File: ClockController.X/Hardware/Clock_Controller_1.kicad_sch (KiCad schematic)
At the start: 3 parts, among them U1 PIC16F15224-I/SL

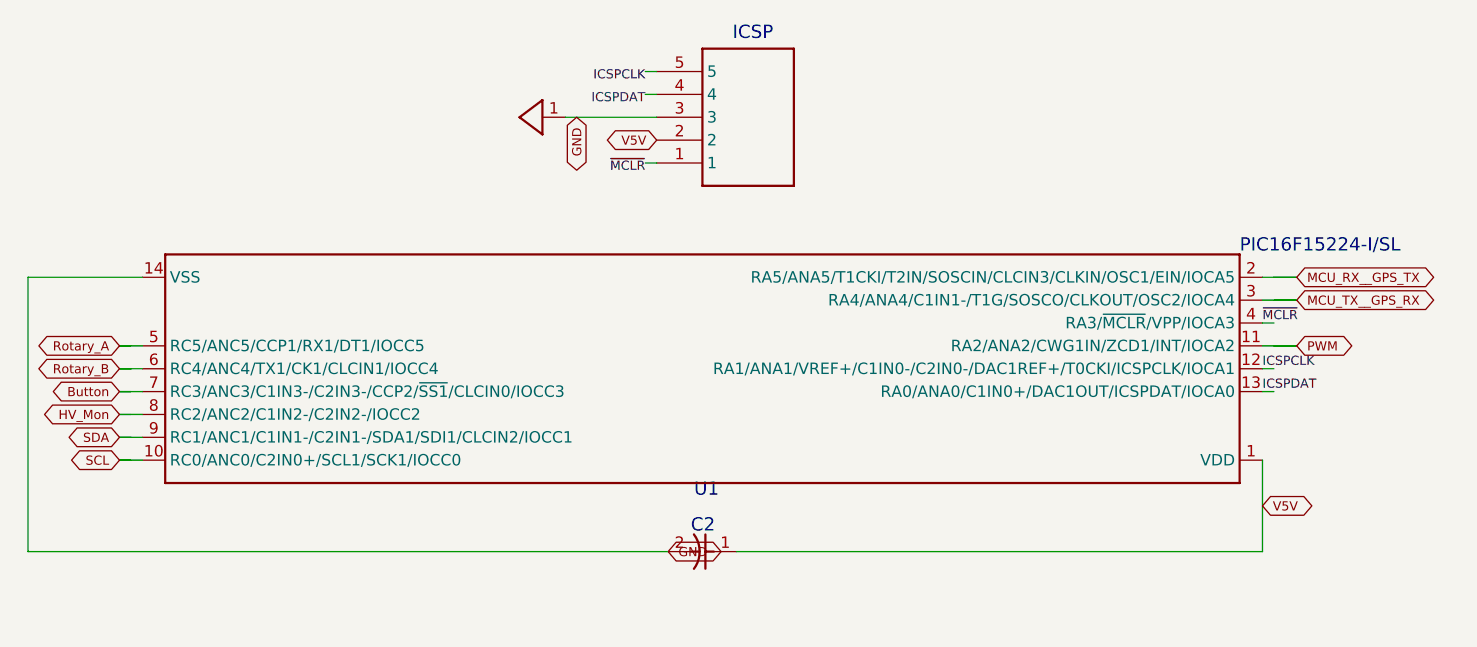
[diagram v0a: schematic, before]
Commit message: Cleaned up a bunch of labels
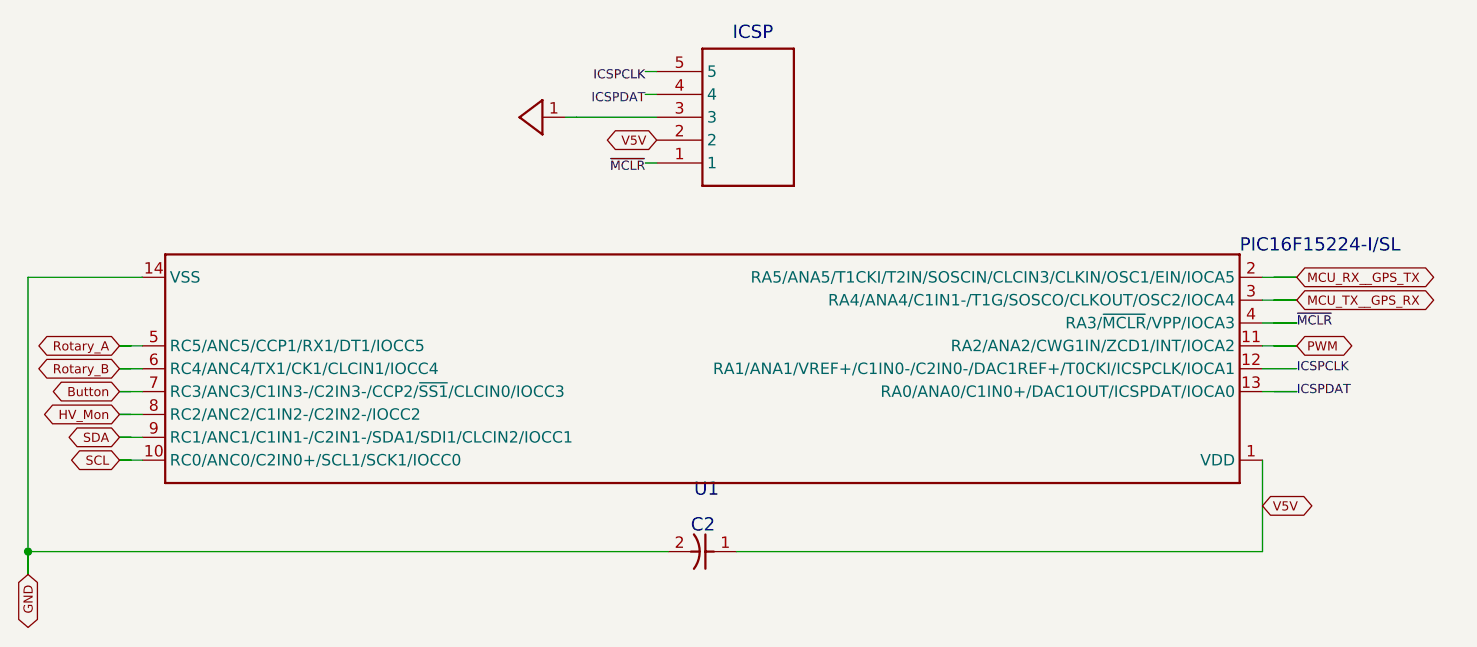
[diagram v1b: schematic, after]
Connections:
- net GND_DIGITAL: no longer C2.2, U1.14 (VSS)
- new net GND: C2.2, U1.14 (VSS)
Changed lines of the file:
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@@
 	(generator_version "8.0")
 	(paper "A4")
+	(junction
+		(at 68.58 130.81)
+		(diameter 0)
+		(color 0 0 0 0)
+	)
+	(wire
+		(pts
+			(xy 68.58 130.81) (xy 139.7 130.81)
+		)
+		(stroke
+			(width 0)
+			(type default)
+		)
+	)
 	(wire
 		(pts
@@
 	(wire
 		(pts
-			(xy 139.7 130.81) (xy 68.58 130.81)
-		)
-		(stroke
-			(width 0.25)
-			(type solid)
-		)
-	)
-	(wire
-		(pts
 			(xy 129.54 82.55) (xy 128.27 82.55)
 		)
@@
 	(wire
 		(pts
+			(xy 209.55 110.49) (xy 205.74 110.49)
+		)
+		(stroke
+			(width 0)
+			(type default)
+		)
+	)
+	(wire
+		(pts
 			(xy 209.55 107.95) (xy 207.01 107.95)
 		)
@@
 	(wire
 		(pts
-			(xy 205.74 110.49) (xy 207.01 110.49)
-		)
-		(stroke
-			(width 0.25)
-			(type solid)
-		)
-	)
-	(wire
-		(pts
 			(xy 209.55 102.87) (xy 207.01 102.87)
 		)
@@
 	(wire
 		(pts
+			(xy 68.58 133.35) (xy 68.58 130.81)
+		)
+		(stroke
+			(width 0.25)
+			(type solid)
+		)
+	)
+	(wire
+		(pts
 			(xy 78.74 118.11) (xy 81.28 118.11)
 		)
@@
 	(wire
 		(pts
-			(xy 205.74 113.03) (xy 207.01 113.03)
+			(xy 209.55 113.03) (xy 207.01 113.03)
 		)
 		(stroke
@@
 	(wire
 		(pts
+			(xy 68.58 133.35) (xy 68.58 130.81)
+		)
+		(stroke
+			(width 0)
+			(type default)
+		)
+	)
+	(wire
+		(pts
 			(xy 209.55 107.95) (xy 205.74 107.95)
 		)
@@
 	(wire
 		(pts
+			(xy 209.55 105.41) (xy 205.74 105.41)
+		)
+		(stroke
+			(width 0)
+			(type default)
+		)
+	)
+	(wire
+		(pts
 			(xy 209.55 100.33) (xy 205.74 100.33)
 		)
@@
 	(wire
 		(pts
+			(xy 209.55 113.03) (xy 205.74 113.03)
+		)
+		(stroke
+			(width 0)
+			(type default)
+		)
+	)
+	(wire
+		(pts
 			(xy 78.74 115.57) (xy 81.28 115.57)
 		)
@@
 	(wire
 		(pts
-			(xy 205.74 105.41) (xy 207.01 105.41)
+			(xy 209.55 105.41) (xy 207.01 105.41)
 		)
 		(stroke
@@
 	)
 	(label "~{MCLR}"
-		(at 205.74 105.41 0)
-		(fields_autoplaced yes)
-		(effects
-			(font
-				(size 1.016 1.016)
-			)
-			(justify left bottom)
+		(at 209.55 105.41 0)
+		(fields_autoplaced yes)
+		(effects
+			(font
+				(size 1.016 1.016)
+			)
+			(justify left)
 		)
 	)
@@
 	)
 	(label "ICSPCLK"
-		(at 205.74 110.49 0)
-		(fields_autoplaced yes)
-		(effects
-			(font
-				(size 1.016 1.016)
-			)
-			(justify left bottom)
+		(at 209.55 110.49 0)
+		(fields_autoplaced yes)
+		(effects
+			(font
+				(size 1.016 1.016)
+			)
+			(justify left)
 		)
 	)
 	(label "ICSPDAT"
-		(at 205.74 113.03 0)
-		(fields_autoplaced yes)
-		(effects
-			(font
-				(size 1.016 1.016)
-			)
-			(justify left bottom)
+		(at 209.55 113.03 0)
+		(fields_autoplaced yes)
+		(effects
+			(font
+				(size 1.016 1.016)
+			)
+			(justify left)
 		)
 	)
@@
 	(global_label "GND"
 		(shape bidirectional)
-		(at 139.7 130.81 0)
+		(at 68.58 133.35 270)
+		(fields_autoplaced yes)
+		(effects
+			(font
+				(size 1.016 1.016)
+			)
+			(justify right)
+		)
+		(property "Intersheetrefs" "${INTERSHEET_REFS}"
+			(at 68.58 139.7233 90)
+			(effects
+				(font
+					(size 1.27 1.27)
+				)
+				(justify right)
+				(hide yes)
+			)
+		)
+	)
+	(global_label "SCL"
+		(shape bidirectional)
+		(at 78.74 120.65 180)
+		(fields_autoplaced yes)
+		(effects
+			(font
+				(size 1.016 1.016)
+			)
+			(justify right)
+		)
+		(property "Intersheetrefs" "${INTERSHEET_REFS}"
+			(at 72.657 120.65 0)
+			(effects
+				(font
+					(size 1.27 1.27)
+				)
+				(justify right)
+				(hide yes)
+			)
+		)
+	)
+	(global_label "HV_Mon"
+		(shape bidirectional)
+		(at 78.74 115.57 180)
+		(fields_autoplaced yes)
+		(effects
+			(font
+				(size 1.016 1.016)
+			)
+			(justify right)
+		)
+		(property "Intersheetrefs" "${INTERSHEET_REFS}"
+			(at 69.7542 115.57 0)
+			(effects
+				(font
+					(size 1.27 1.27)
+				)
+				(justify right)
+				(hide yes)
+			)
+		)
+	)
+	(global_label "Rotary_A"
+		(shape bidirectional)
+		(at 78.74 107.95 180)
+		(fields_autoplaced yes)
+		(effects
+			(font
+				(size 1.016 1.016)
+			)
+			(justify right)
+		)
+		(property "Intersheetrefs" "${INTERSHEET_REFS}"
+			(at 68.98 107.95 0)
+			(effects
+				(font
+					(size 1.27 1.27)
+				)
+				(justify right)
+				(hide yes)
+			)
+		)
+	)
+	(global_label "Rotary_B"
+		(shape bidirectional)
+		(at 78.74 110.49 180)
+		(fields_autoplaced yes)
+		(effects
+			(font
+				(size 1.016 1.016)
+			)
+			(justify right)
+		)
+		(property "Intersheetrefs" "${INTERSHEET_REFS}"
+			(at 68.8349 110.49 0)
+			(effects
+				(font
+					(size 1.27 1.27)
+				)
+				(justify right)
+				(hide yes)
+			)
+		)
+	)
+	(global_label "PWM"
+		(shape bidirectional)
+		(at 209.55 107.95 0)
 		(fields_autoplaced yes)
 		(effects
@@
 		)
 		(property "Intersheetrefs" "${INTERSHEET_REFS}"
-			(at 146.0733 130.81 0)
+			(at 216.1651 107.95 0)
 			(effects
 				(font
@@
 				(hide yes)
 			)
-		)
-	)
-	(global_label "SCL"
-		(shape bidirectional)
-		(at 78.74 120.65 180)
-		(fields_autoplaced yes)
-		(effects
-			(font
-				(size 1.016 1.016)
-			)
-			(justify right)
-		)
-		(property "Intersheetrefs" "${INTERSHEET_REFS}"
-			(at 72.657 120.65 0)
-			(effects
-				(font
-					(size 1.27 1.27)
-				)
-				(justify right)
-				(hide yes)
-			)
-		)
-	)
-	(global_label "HV_Mon"
-		(shape bidirectional)
-		(at 78.74 115.57 180)
-		(fields_autoplaced yes)
-		(effects
-			(font
-				(size 1.016 1.016)
-			)
-			(justify right)
-		)
-		(property "Intersheetrefs" "${INTERSHEET_REFS}"
-			(at 69.7542 115.57 0)
-			(effects
-				(font
-					(size 1.27 1.27)
-				)
-				(justify right)
-				(hide yes)
-			)
-		)
-	)
-	(global_label "Rotary_A"
-		(shape bidirectional)
-		(at 78.74 107.95 180)
-		(fields_autoplaced yes)
-		(effects
-			(font
-				(size 1.016 1.016)
-			)
-			(justify right)
-		)
-		(property "Intersheetrefs" "${INTERSHEET_REFS}"
-			(at 68.98 107.95 0)
-			(effects
-				(font
-					(size 1.27 1.27)
-				)
-				(justify right)
-				(hide yes)
-			)
-		)
-	)
-	(global_label "Rotary_B"
-		(shape bidirectional)
-		(at 78.74 110.49 180)
-		(fields_autoplaced yes)
-		(effects
-			(font
-				(size 1.016 1.016)
-			)
-			(justify right)
-		)
-		(property "Intersheetrefs" "${INTERSHEET_REFS}"
-			(at 68.8349 110.49 0)
-			(effects
-				(font
-					(size 1.27 1.27)
-				)
-				(justify right)
-				(hide yes)
-			)
-		)
-	)
-	(global_label "PWM"
-		(shape bidirectional)
-		(at 209.55 107.95 0)
-		(fields_autoplaced yes)
-		(effects
-			(font
-				(size 1.016 1.016)
-			)
-			(justify left)
-		)
-		(property "Intersheetrefs" "${INTERSHEET_REFS}"
-			(at 216.1651 107.95 0)
-			(effects
-				(font
-					(size 1.27 1.27)
-				)
-				(justify left)
-				(hide yes)
-			)
-		)
-	)
-	(global_label "GND"
-		(shape bidirectional)
-		(at 129.54 82.55 270)
-		(fields_autoplaced yes)
-		(effects
-			(font
-				(size 1.016 1.016)
-			)
-			(justify right)
-		)
-		(property "Intersheetrefs" "${INTERSHEET_REFS}"
-			(at 129.54 88.9233 90)
-			(effects
-				(font
-					(size 1.27 1.27)
-				)
-				(justify right)
-				(hide yes)
-			)
